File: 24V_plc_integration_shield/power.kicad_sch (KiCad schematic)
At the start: 9 parts, among them J2 USB_A_Stacked, J4 Screw_Terminal_01x02, J5 Conn_01x02_Female, U4 JTD2024S05

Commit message: 4 layer design
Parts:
- D1: footprint LED_THT:LED_D5.0mm -> LED_SMD:LED_0805_2012Metric_Pad1.15x1.40mm_HandSolder
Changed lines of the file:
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@@
     (property "Reference" "D1" (id 0) (at 140.97 92.71 90))
     (property "Value" "Green 20 mA 2.2 Vf" (id 1) (at 157.48 92.71 90))
-    (property "Footprint" "LED_THT:LED_D5.0mm" (id 2) (at 144.78 92.71 0)
+    (property "Footprint" "LED_SMD:LED_0805_2012Metric_Pad1.15x1.40mm_HandSolder" (id 2) (at 144.78 92.71 0)
       (effects (font (size 1.27 1.27)) hide)
     )

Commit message: pcb v3 presentation ready
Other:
- company: (none) -> ${company}
- title: (none) -> ${project_title} - ${board_title}
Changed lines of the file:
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@@
   (paper "A4")
   (title_block
-    (date "2022-03-15")
-    (rev "v2.2pre")
+    (title "${project_title} - ${board_title}")
+    (date "2022-03-23")
+    (rev "${git_describe}")
+    (company "${company}")
+    (comment 1 "${drawn_by}")
+    (comment 4 "${git_url}")
   )
   (junction (at 86.36 88.9) (diameter 0) (color 0 0 0 0)

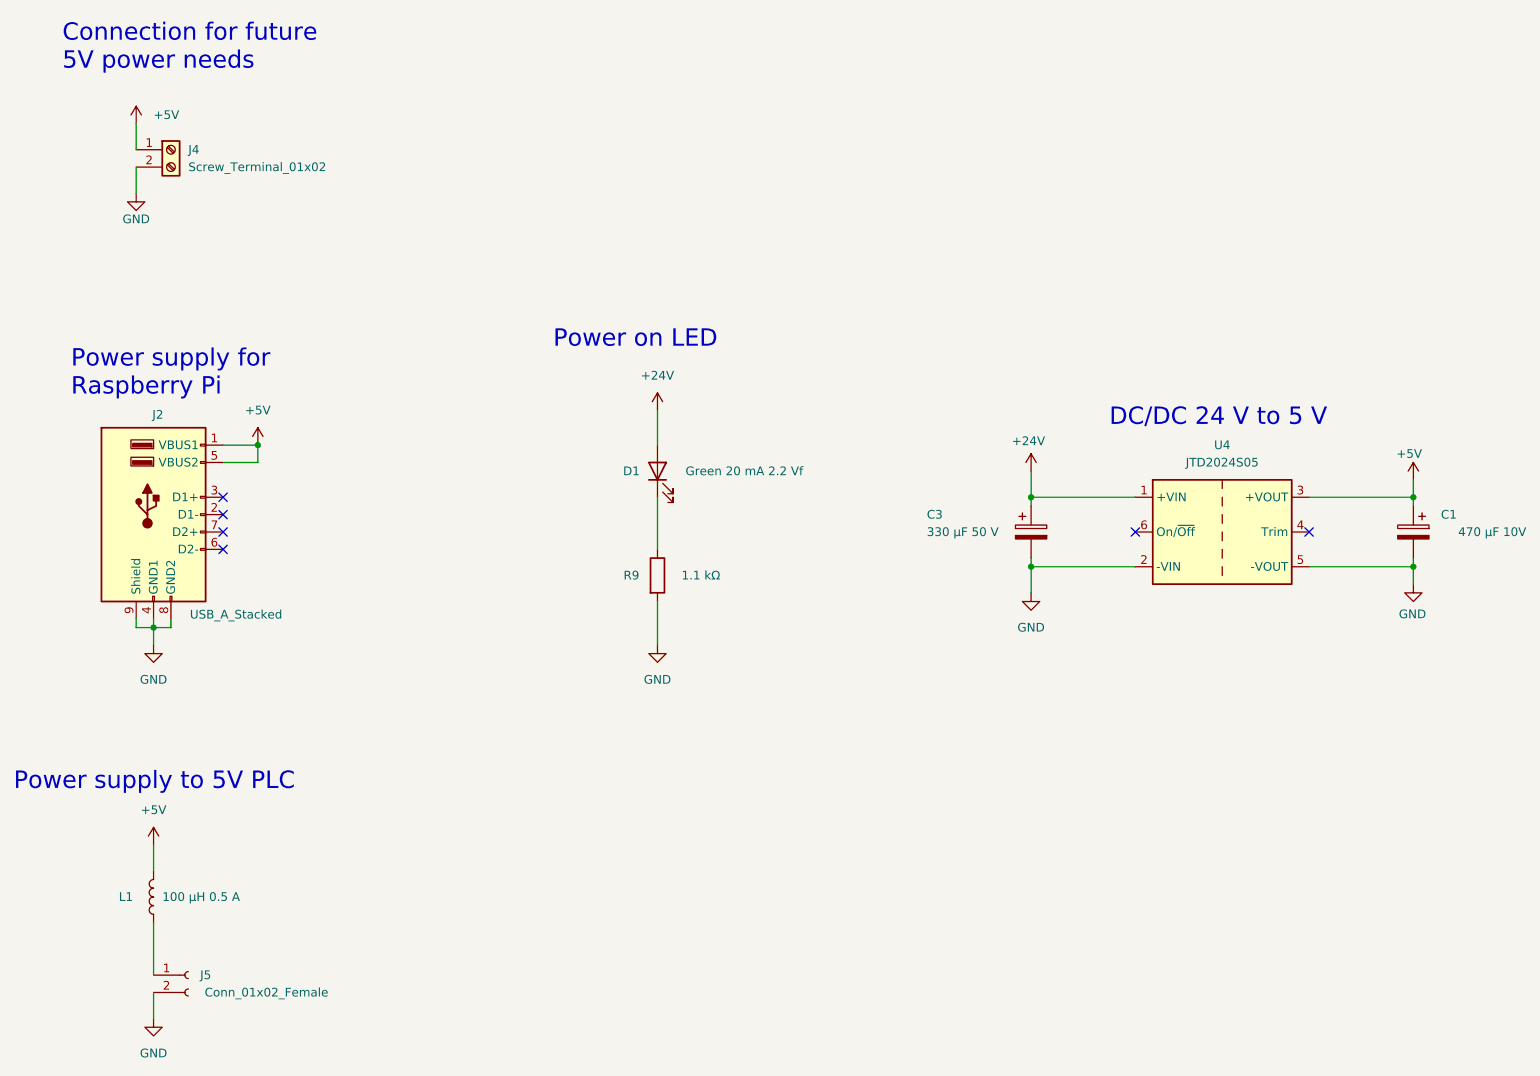
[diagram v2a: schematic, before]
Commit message: update for integration into clay_3dp_wiring sheet
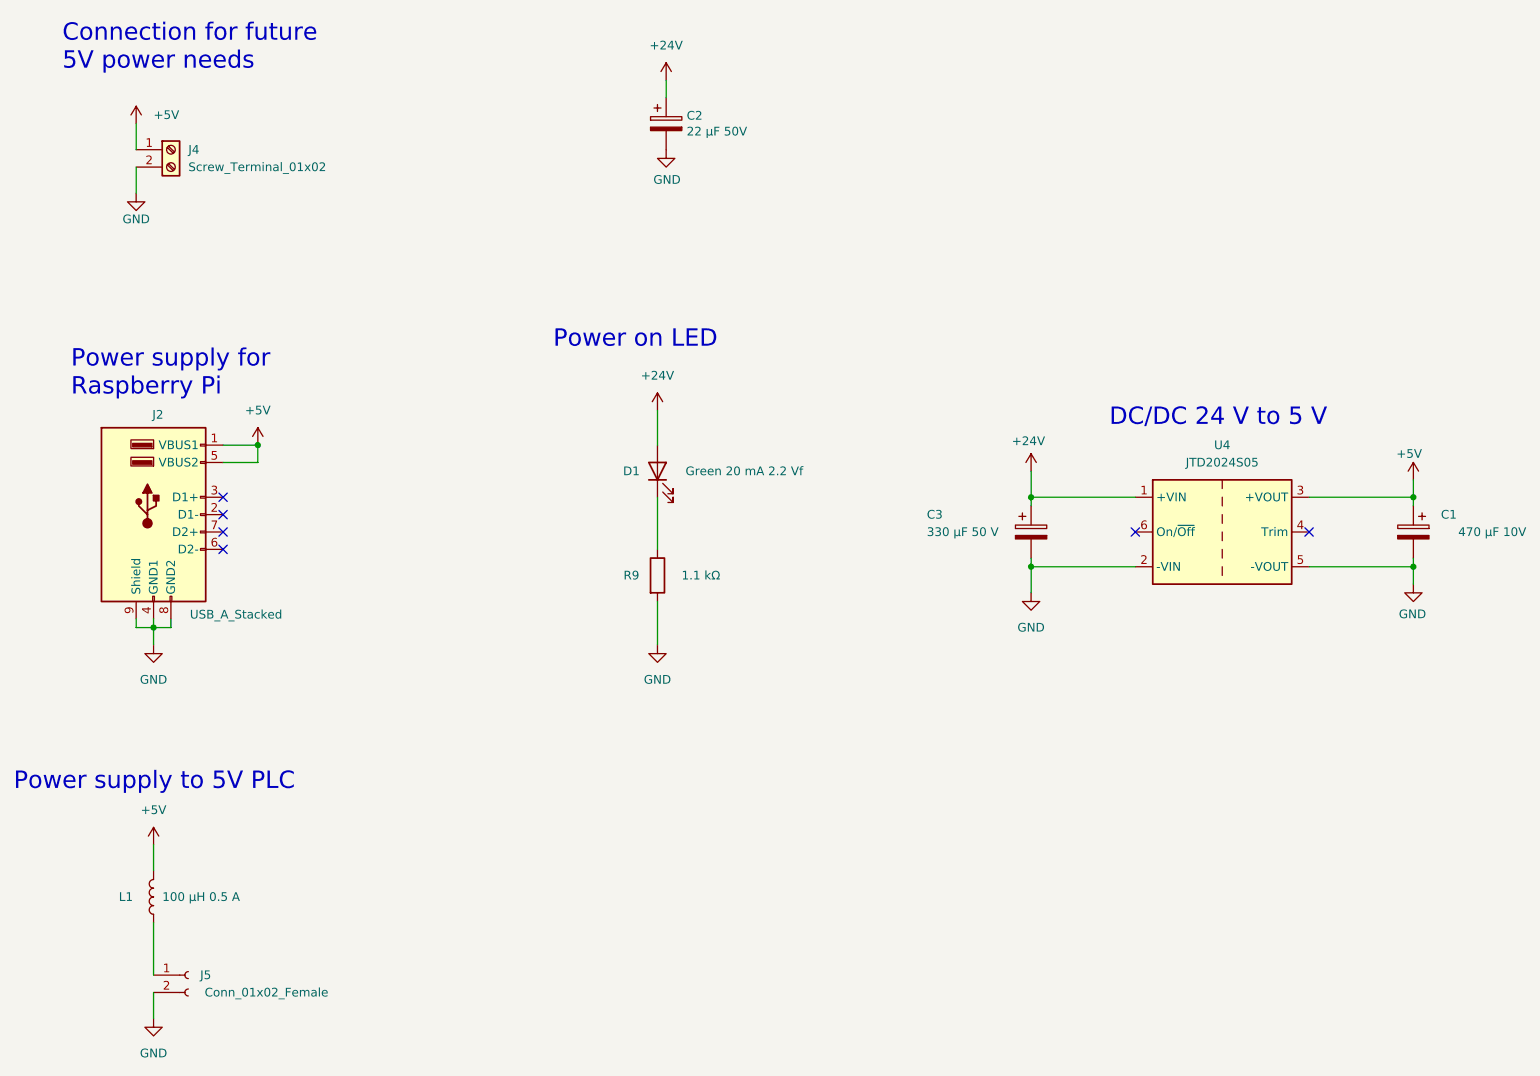
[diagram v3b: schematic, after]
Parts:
- added C2: 22 µF 50V, Capacitor_THT:CP_Radial_D5.0mm_P2.00mm, symbol Device:C_Polarized
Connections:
- net +24V: now also C2.1
- net GND: now also C2.2

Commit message: fixes in regards to refs
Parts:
- J5: value Conn_01x02_Female -> Conn_01x02_Socket; symbol Connector:Conn_01x02_Female -> Connector:Conn_01x02_Socket
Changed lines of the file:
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@@
+          (reference "#PWR0104") (unit 1)
+        )
+        (path "/9538e4ed-27e6-4c37-b989-9859dc0d49e8/15acb311-fc6d-4dca-ab5d-737ef8928bc0"
           (reference "#PWR0104") (unit 1)
         )
@@
     )
   )
-  (symbol (lib_id "Connector:Conn_01x02_Female") (at 76.2 166.37 0) (unit 1)
+  (symbol (lib_id "Connector:Conn_01x02_Socket") (at 76.2 166.37 0) (unit 1)
     (in_bom yes) (on_board yes) (dnp no)
     (property "Reference" "J5" (at 78.74 166.37 0)
       (effects (font (size 1.27 1.27)))
     )
-    (property "Value" "Conn_01x02_Female" (at 87.63 168.91 0)
+    (property "Value" "Conn_01x02_Socket" (at 86.36 168.91 0)
       (effects (font (size 1.27 1.27)))
     )
@@
       (project "24V_plc_integration_shield"
         (path "/9538e4ed-27e6-4c37-b989-9859dc0d49e8/15acb311-fc6d-4dca-ab5d-737ef8928bc0"
-          (reference "#PWR0116") (unit 1)
+          (reference "#PWR0102") (unit 1)
         )
       )
@@
           (reference "C2") (unit 1)
         )
+        (path "/9538e4ed-27e6-4c37-b989-9859dc0d49e8/15acb311-fc6d-4dca-ab5d-737ef8928bc0"
+          (reference "C2") (unit 1)
+        )
